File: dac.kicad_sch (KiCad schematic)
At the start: 34 parts

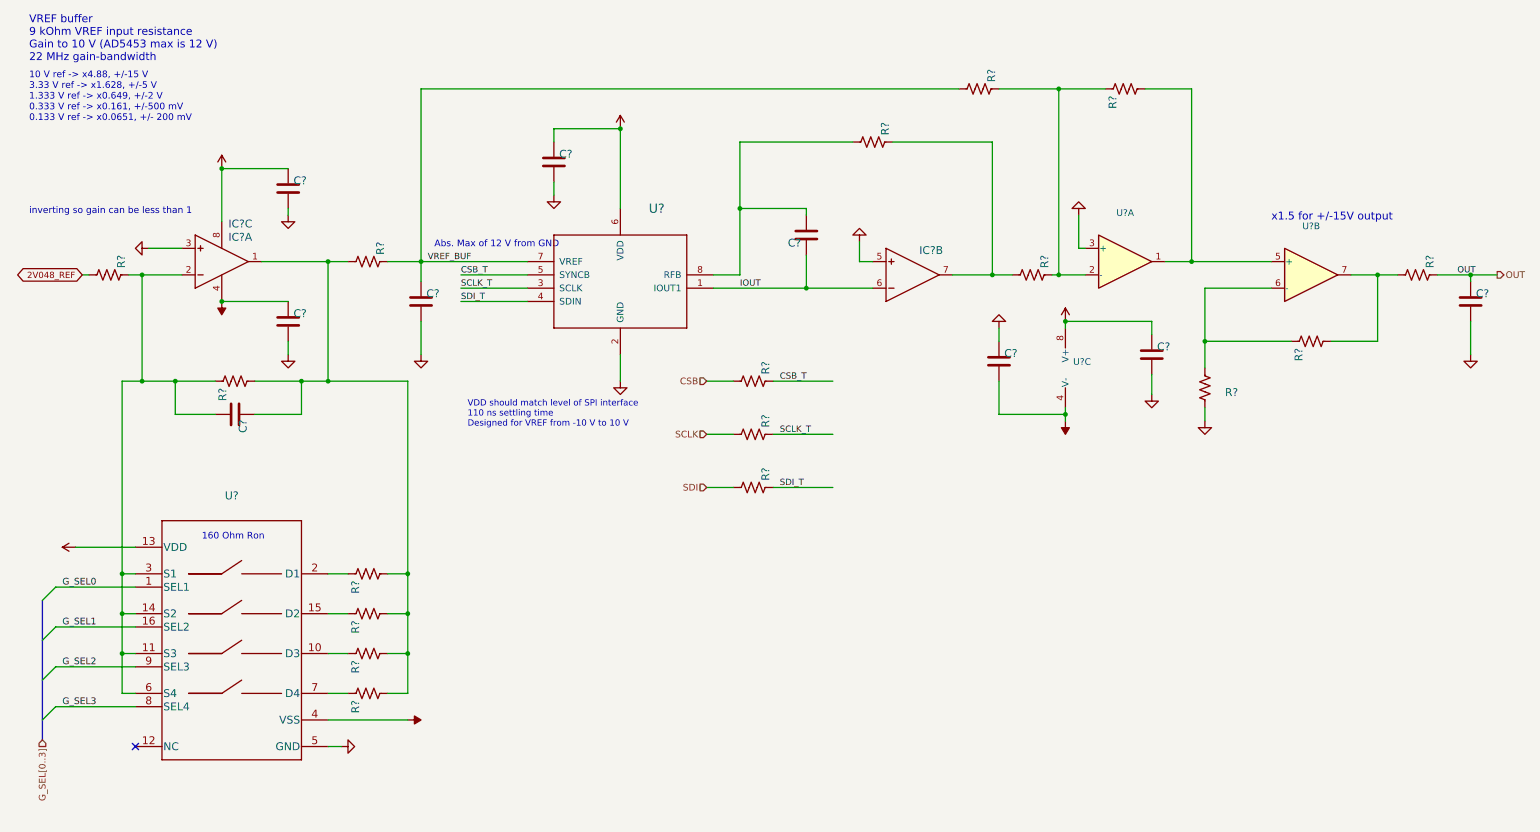
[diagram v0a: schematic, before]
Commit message: closes #31 - incorrect text on Howland current pump. Also, updated fast DAC symbol but not closing until layout is corrected
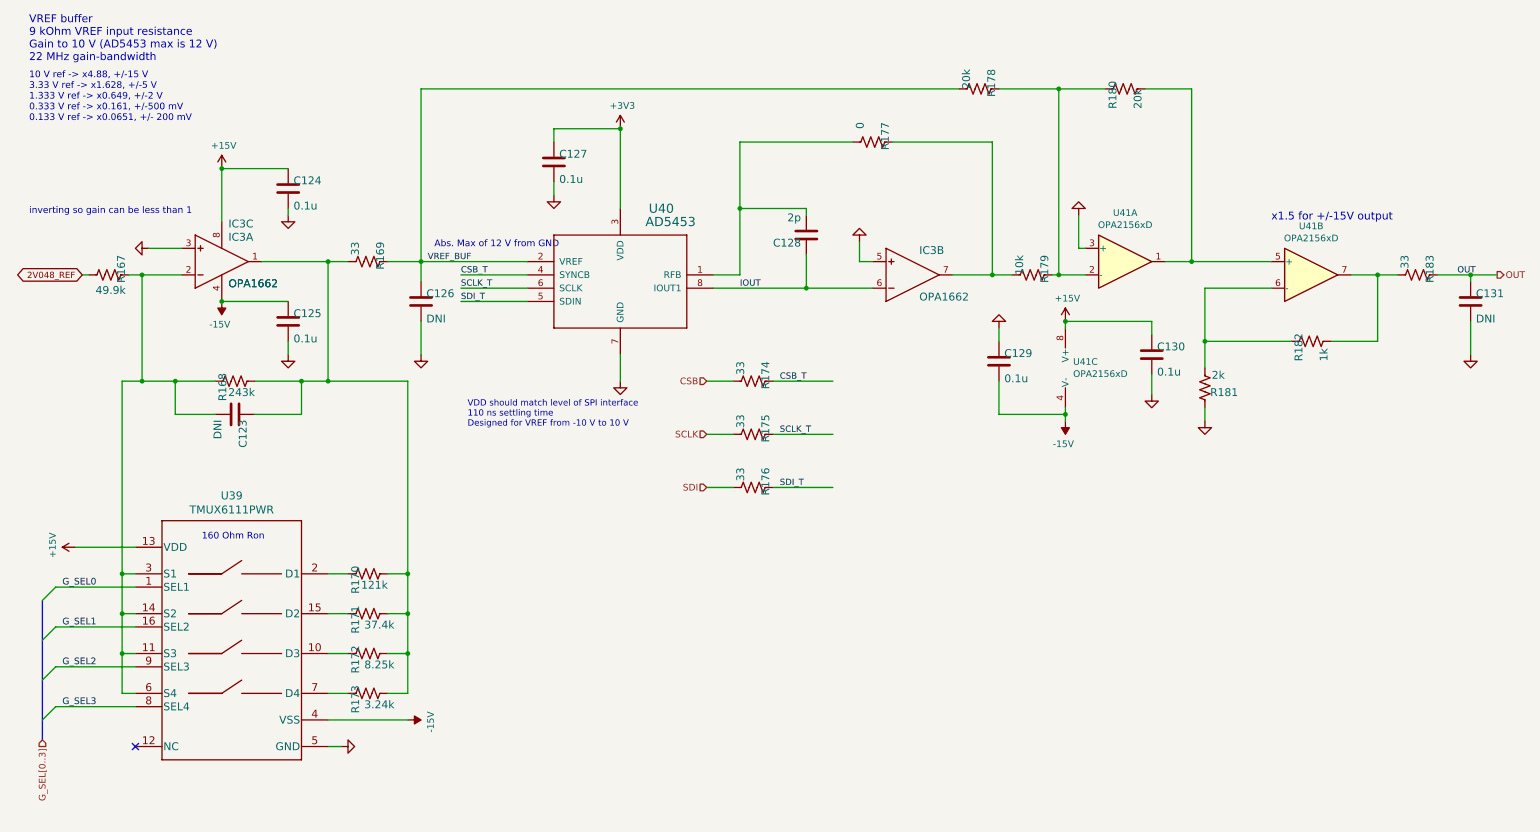
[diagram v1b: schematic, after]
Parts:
- C123, C126, C131: renamed from C?; value (none) -> DNI; footprint (none) -> Capacitor_SMD:C_0603_1608Metric
- C124, C125, C127, C129, C130: renamed from C?; value (none) -> 0.1u; footprint (none) -> Capacitor_SMD:C_0603_1608Metric
- C128: renamed from C?; value (none) -> 2p; footprint (none) -> Capacitor_SMD:C_0603_1608Metric
- IC3: renamed from IC?; value (none) -> OPA1662; footprint (none) -> Package_SO:VSSOP-8_3.0x3.0mm_P0.65mm
- R167: renamed from R?; value (none) -> 49.9k; footprint (none) -> Resistor_SMD:R_0603_1608Metric
- R168: renamed from R?; value (none) -> 243k; footprint (none) -> Resistor_SMD:R_0603_1608Metric
- R169, R174, R175, R176, R183: renamed from R?; value (none) -> 33; footprint (none) -> Resistor_SMD:R_0603_1608Metric
- R170: renamed from R?; value (none) -> 121k; footprint (none) -> Resistor_SMD:R_0603_1608Metric
- R171: renamed from R?; value (none) -> 37.4k; footprint (none) -> Resistor_SMD:R_0603_1608Metric
- R172: renamed from R?; value (none) -> 8.25k; footprint (none) -> Resistor_SMD:R_0603_1608Metric
- R173: renamed from R?; value (none) -> 3.24k; footprint (none) -> Resistor_SMD:R_0603_1608Metric
- R177: renamed from R?; value (none) -> 0; footprint (none) -> Resistor_SMD:R_0603_1608Metric
- R178, R180: renamed from R?; value (none) -> 20k; footprint (none) -> Resistor_SMD:R_0603_1608Metric
- R179: renamed from R?; value (none) -> 10k; footprint (none) -> Resistor_SMD:R_0603_1608Metric
- R181: renamed from R?; value (none) -> 2k; footprint (none) -> Resistor_SMD:R_0603_1608Metric
- R182: renamed from R?; value (none) -> 1k; footprint (none) -> Resistor_SMD:R_0603_1608Metric
- U39: renamed from U?; value (none) -> TMUX6111PWR; footprint (none) -> Package_SO:TSSOP-16_4.4x5mm_P0.65mm
- U40: renamed from U?; value (none) -> AD5453; footprint (none) -> Package_TO_SOT_SMD:TSOT-23-8; symbol covg-kicad:AD5453 -> covg-kicad:AD5453{colon}TSOT
- U41: renamed from U?; value (none) -> OPA2156xD; footprint (none) -> Package_SO:SOIC-8_3.9x4.9mm_P1.27mm
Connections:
- net +3V3: now also U40.3 (VDD); no longer U40.6 (VDD)
- net CSB_T: now also U40.4 (SYNCB); no longer U40.5 (SYNCB)
- net GND: now also U40.7 (GND); no longer U40.2 (GND)
- net IOUT: now also U40.8 (IOUT1); no longer U40.1 (IOUT1)
- net SCLK_T: now also U40.6 (SCLK); no longer U40.3 (SCLK)
- net SDI_T: now also U40.5 (SDIN); no longer U40.4 (SDIN)
- net VREF_BUF: now also U40.2 (VREF); no longer U40.7 (VREF)
- net at C128.2, R177.2: now also U40.1 (RFB); no longer U40.8 (RFB)

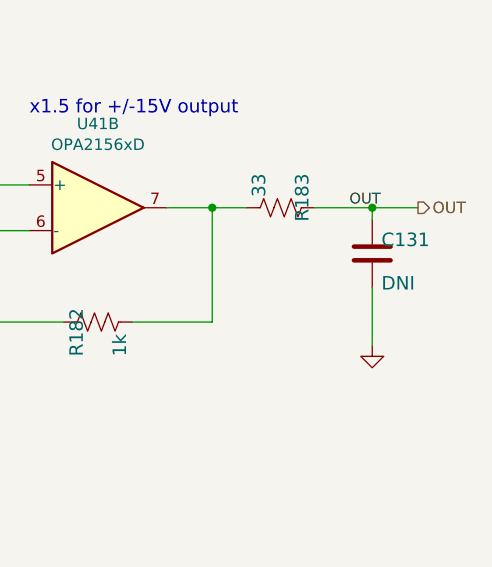
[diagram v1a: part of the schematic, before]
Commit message: added fast DAC output capacitor of 2.4nF and removed filtering caps at ADS8686 input. Closes #22 and Closes #24
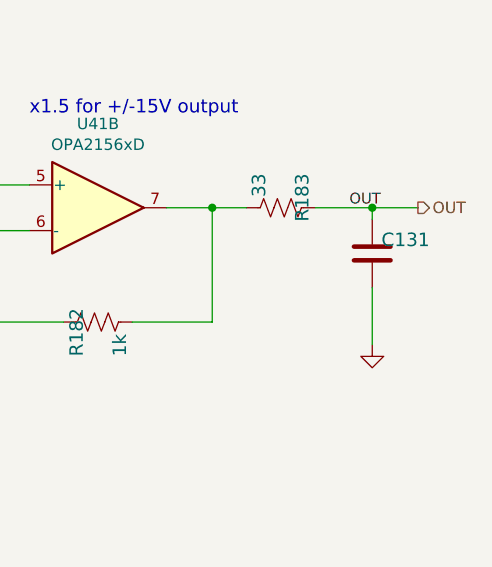
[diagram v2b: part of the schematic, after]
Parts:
- C131: value DNI -> (none); footprint Capacitor_SMD:C_0603_1608Metric -> (none); Manf# (none) -> GRM1885C1H242JA01D; Voltage (none) -> 50
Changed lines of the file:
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@@
       (effects (font (size 1.4986 1.4986)) (justify left bottom))
     )
-    (property "Value" "DNI" (id 1) (at 290.576 72.771 0)
+    (property "Value" "" (id 1) (at 290.576 72.771 0)
       (effects (font (size 1.4986 1.4986)) (justify left bottom))
     )
-    (property "Footprint" "Capacitor_SMD:C_0603_1608Metric" (id 2) (at 289.56 68.58 0)
+    (property "Footprint" "" (id 2) (at 289.56 68.58 0)
       (effects (font (size 1.27 1.27)) hide)
     )
@@
       (effects (font (size 1.27 1.27)) hide)
     )
+    (property "Manf#" "GRM1885C1H242JA01D" (id 4) (at 289.56 68.58 0)
+      (effects (font (size 1.27 1.27)) hide)
+    )
+    (property "Voltage" "50" (id 5) (at 289.56 68.58 0)
+      (effects (font (size 1.27 1.27)) hide)
+    )

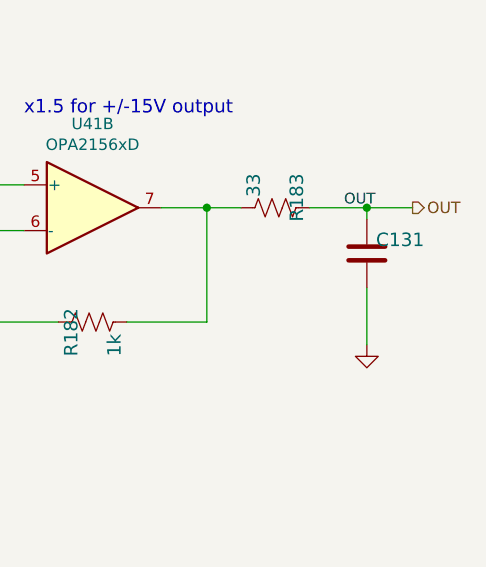
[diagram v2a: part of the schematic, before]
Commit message: Closes #29 full-scale range will be nearly 8uA
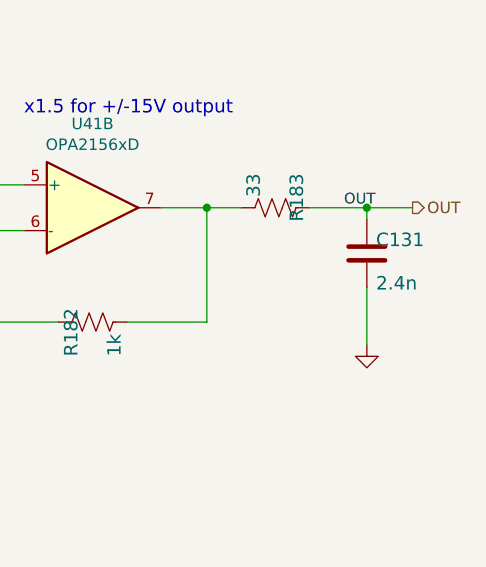
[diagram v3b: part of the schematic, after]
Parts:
- C131: value (none) -> 2.4n; footprint (none) -> Capacitor_SMD:C_0603_1608Metric
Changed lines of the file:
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@@
       (effects (font (size 1.4986 1.4986)) (justify left bottom))
     )
-    (property "Value" "" (id 1) (at 290.576 72.771 0)
+    (property "Value" "2.4n" (id 1) (at 290.576 72.771 0)
       (effects (font (size 1.4986 1.4986)) (justify left bottom))
     )
-    (property "Footprint" "" (id 2) (at 289.56 68.58 0)
+    (property "Footprint" "Capacitor_SMD:C_0603_1608Metric" (id 2) (at 289.56 68.58 0)
       (effects (font (size 1.27 1.27)) hide)
     )
